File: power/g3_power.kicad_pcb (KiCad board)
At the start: 4 copper layers, 50 x 40 mm, 55 parts, among them J101 533980271_Molex, J102 533980271_Molex, J103 53398-0871, SW1 SW_Push, U101 RT9471GQW, U102 TPS61202DRC, U103 LM358, U104 MCP3422

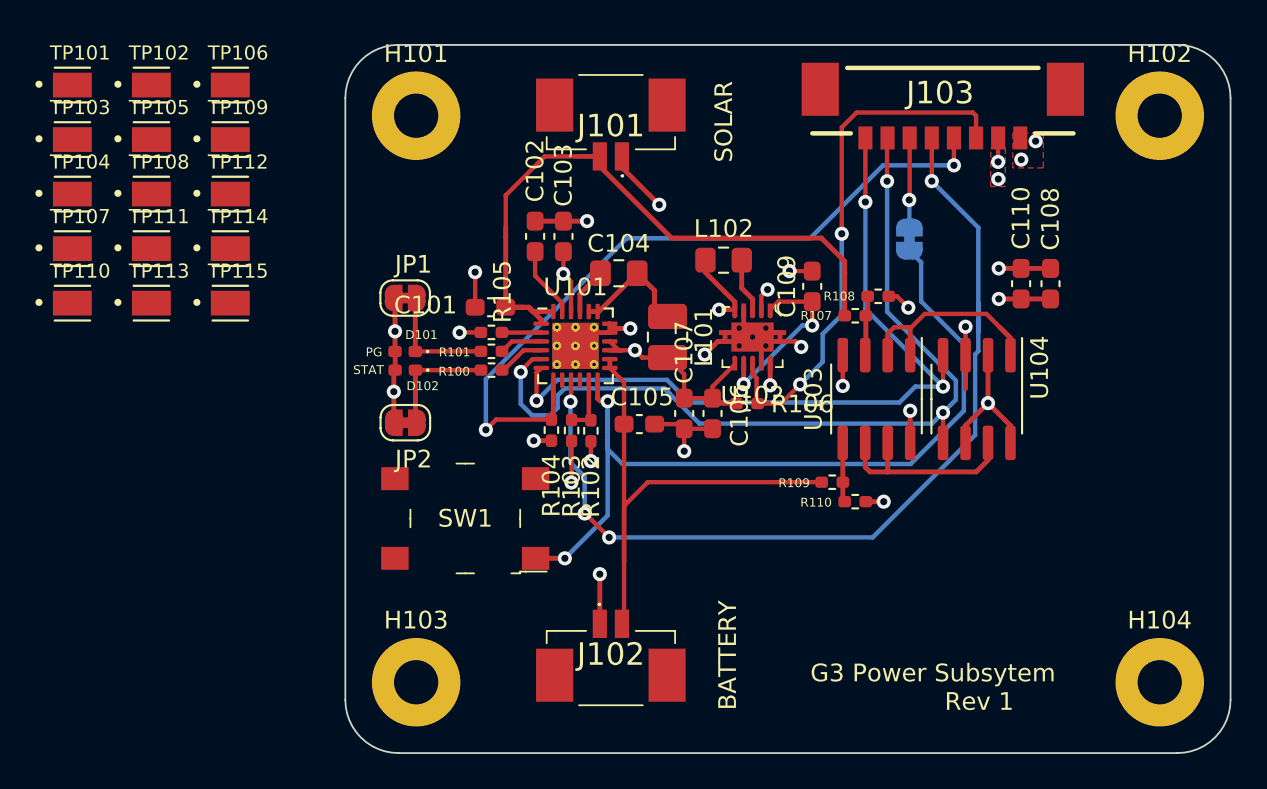
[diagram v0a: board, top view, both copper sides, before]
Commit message: Clearing up reference designators
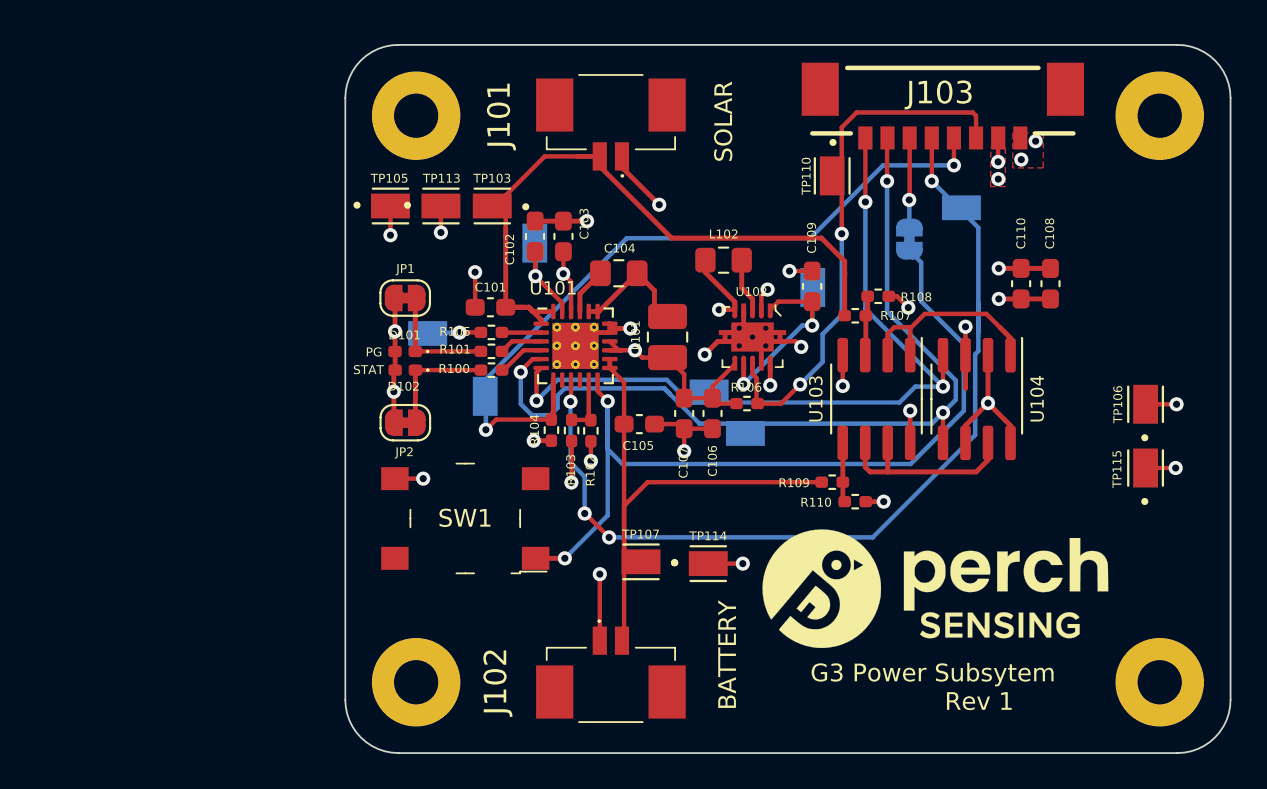
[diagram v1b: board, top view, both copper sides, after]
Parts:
- added G***: LOGO, Perch:perch_logo, F.Cu at (242.4, 100.8)
- TP101, TP102, TP104, TP108, TP109, TP111, TP112: moved to B.Cu
- moved TP106 54.7 mm to (254.2, 90.3), turned to 90 degrees
- moved TP115 52.5 mm to (254.2, 93.9), turned to 90 degrees
- moved TP110 43.5 mm to (236.5, 77.4), turned to 270 degrees
- moved TP101 43.3 mm to (235.4, 83.7), turned to 90 degrees
- moved TP112 41.3 mm to (243.8, 79.2)
- moved TP107 36.7 mm to (225.7, 99.2), turned to 180 degrees
- moved TP108 36.2 mm to (231.6, 92.0), turned to 180 degrees
- moved TP114 32.3 mm to (229.5, 99.3)
- moved TP109 30.6 mm to (229.6, 89.6), turned to 180 degrees
- moved TP104 26.3 mm to (219.7, 81.2), turned to 90 degrees
- moved TP103 24.0 mm to (217.3, 79.1), turned to 180 degrees
- moved TP102 21.0 mm to (213.7, 86.3)
- moved TP111 20.6 mm to (216.9, 89.8), turned to 90 degrees
- moved TP113 17.3 mm to (214.4, 79.1)
- moved TP105 14.0 mm to (211.6, 79.1)
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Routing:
- net GND: track 51.2 -> 58.9 mm, vias 17 -> 21
- net BOOST_VAUX: track 10.3 -> 12.4 mm
- net CC_PWR_OUT: track 20.2 -> 22.1 mm
- net CC_PIMD: track 4.02 -> 5.89 mm, vias 0 -> 1
- net +5V: track 10.7 -> 12.4 mm, vias 7 -> 8
- net V_REGN: track 11.8 -> 13.4 mm, vias 4 -> 5
- net V_BATT: track 30.2 -> 31.1 mm
- net /CC_SDA: track 43.9 -> 44.6 mm
- net /CC_SCL: track 49.2 -> 49.9 mm
- net /BOOST_PS: track 29.9 -> 30.6 mm

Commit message: Labeling testpoints
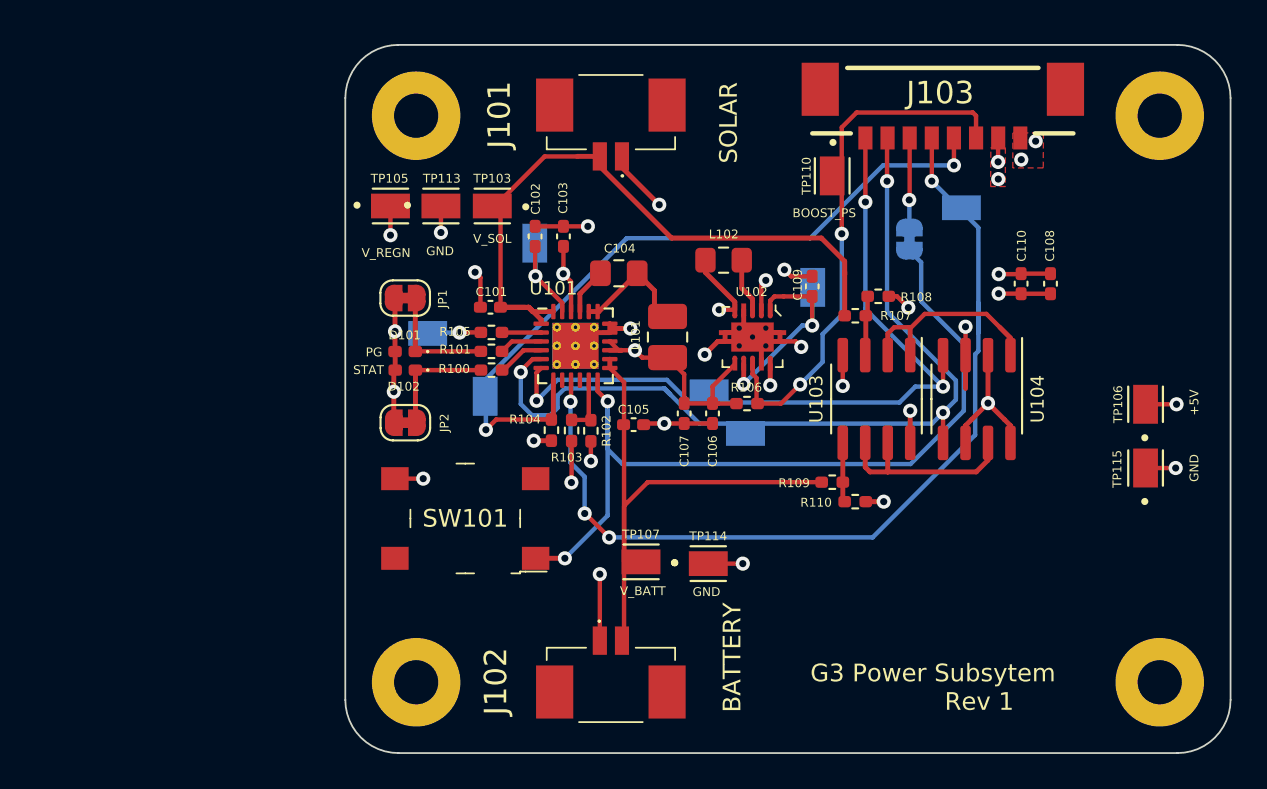
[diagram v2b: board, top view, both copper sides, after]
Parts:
- removed G***: LOGO, Perch:perch_logo
- C101, C102, C103, C105, C106, C107, C108, C109, C110: footprint Capacitor_SMD:C_0603_1608Metric_Pad1.08x0.95mm_HandSolder -> Capacitor_SMD:C_0402_1005Metric_Pad0.74x0.62mm_HandSolder
- moved C105 0.33 mm to (225.3, 91.5)
- renumbered SW1 to SW101
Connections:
- net /CC_SCL renamed /SCL
- net /CC_SDA renamed /SDA
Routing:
- net V_SOL: track 38.4 -> 37.4 mm
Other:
- board text added: "+5V"
- board text added: "BOOST_PS"
- board text added: "BOOST_VAUX"
- board text added: "CC_PIMD"
- board text added: "CC_PWR_OUT"
- board text added: "GND"
- board text added: "SCL"
- board text added: "SDA"
- board text added: "V_BATT"
- board text added: "V_REGN"
- board text added: "V_SOL"
- board text added: "~CC_CE"
- board text added: "~CC_INT"
